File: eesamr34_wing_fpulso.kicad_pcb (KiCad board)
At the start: 2 copper layers, 50 x 24.9 mm, 19 parts, among them J3 Conn_01x02_Male, P1 SolderJumper_3_Bridged12, Q1 BS250, U2 4069

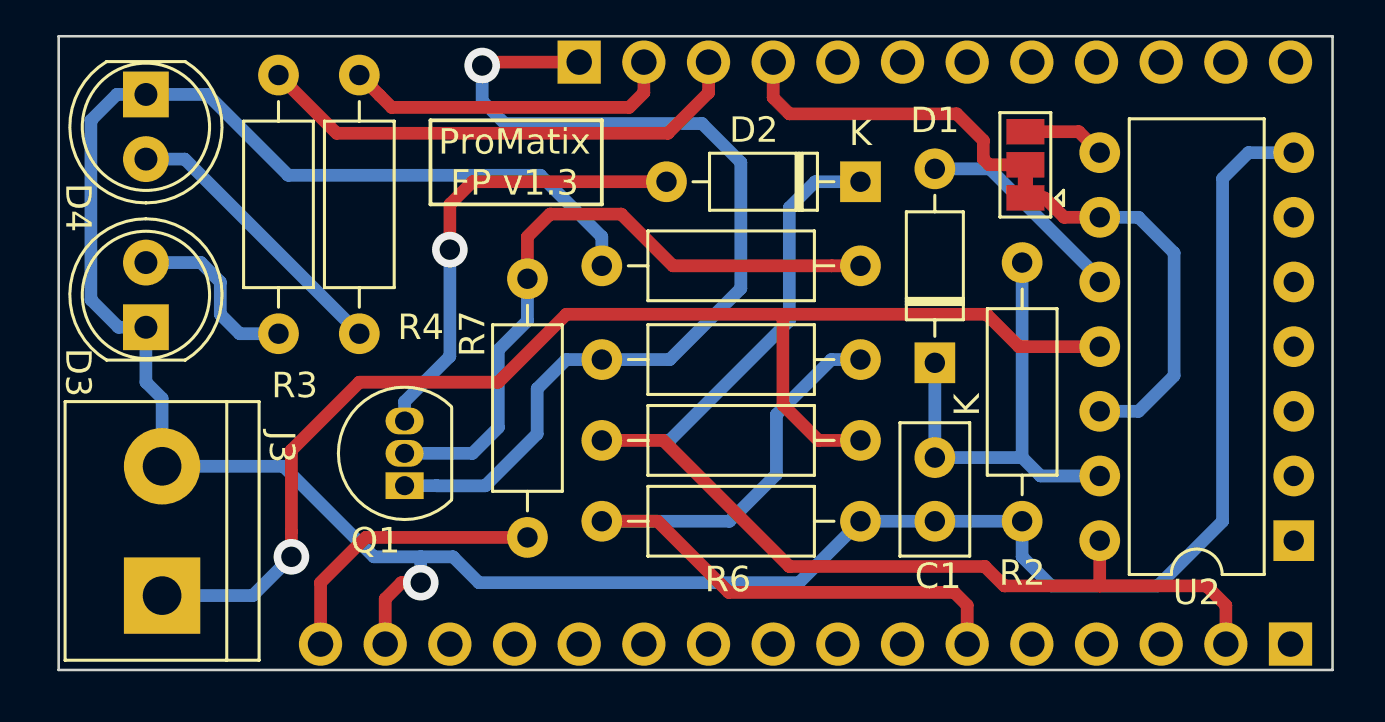
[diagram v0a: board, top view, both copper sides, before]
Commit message: entradas no usadas a 0
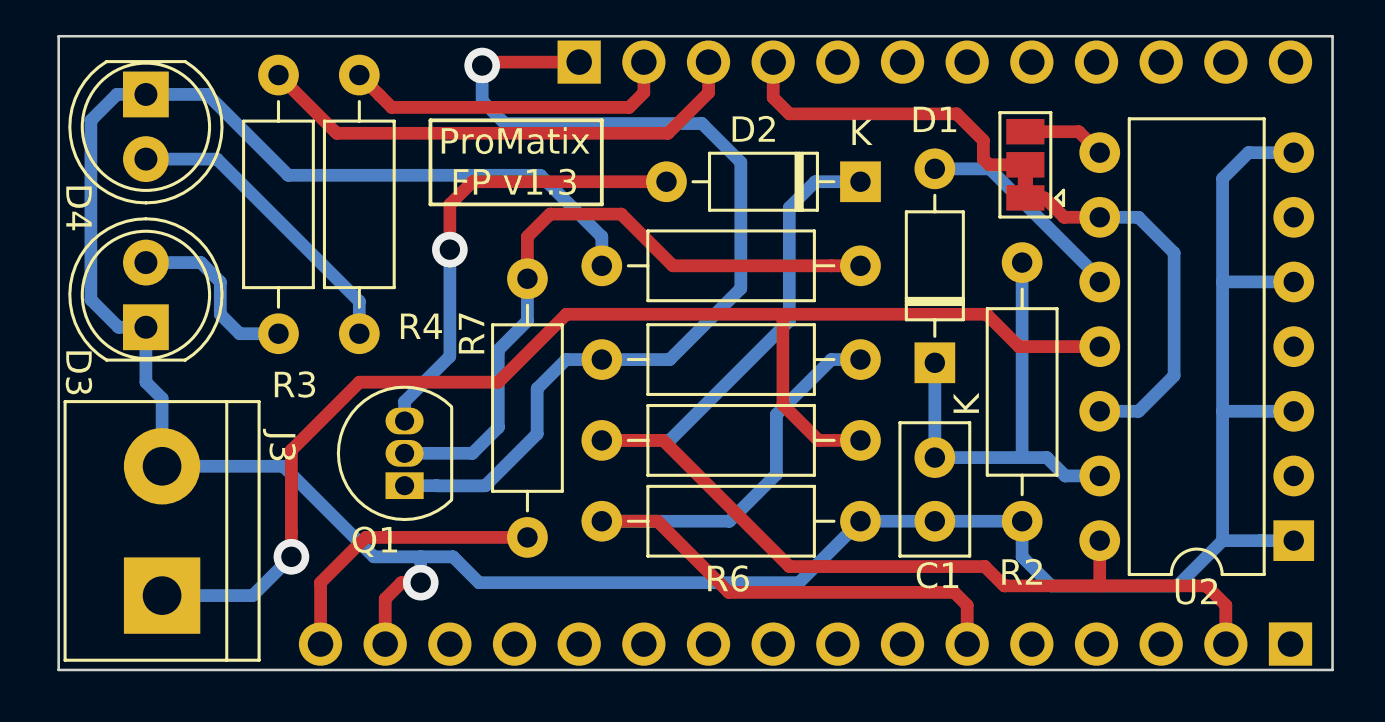
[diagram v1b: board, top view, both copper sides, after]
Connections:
- U2 pad 1: Net-(U2-Pad1) -> GND
- U2 pad 3: Net-(U2-Pad3) -> GND
- U2 pad 5: Net-(U2-Pad5) -> GND
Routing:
- net GND: track 107.9 -> 116.8 mm
- net Net-(D4-Pad2): track 11.2 -> 12.0 mm
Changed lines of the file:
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@@
     (thickness 1.6)
     (drawings 12)
-    (tracks 153)
+    (tracks 161)
     (zones 0)
     (modules 19)
-    (nets 44)
+    (nets 41)
   )
   (page A4 portrait)
@@
     (0 F.Cu signal)
     (31 B.Cu signal)
-    (32 B.Adhes user hide)
-    (33 F.Adhes user hide)
-    (34 B.Paste user hide)
-    (35 F.Paste user hide)
+    (32 B.Adhes user)
+    (33 F.Adhes user)
+    (34 B.Paste user)
+    (35 F.Paste user)
     (36 B.SilkS user)
     (37 F.SilkS user)
     (38 B.Mask user)
-    (39 F.Mask user hide)
+    (39 F.Mask user)
     (40 Dwgs.User user)
     (41 Cmts.User user)
@@
     (43 Eco2.User user)
     (44 Edge.Cuts user)
-    (45 Margin user hide)
+    (45 Margin user)
     (46 B.CrtYd user)
     (47 F.CrtYd user)
-    (48 B.Fab user hide)
-    (49 F.Fab user hide)
+    (48 B.Fab user)
+    (49 F.Fab user)
   )
   (setup
-    (last_trace_width 0.8)
+    (last_trace_width 0.5)
     (user_trace_width 0.5)
     (user_trace_width 0.8)
@@
   (net 36 /ADC7)
   (net 37 "Net-(Q1-Pad2)")
-  (net 38 "Net-(U2-Pad3)")
-  (net 39 "Net-(U2-Pad4)")
-  (net 40 "Net-(U2-Pad1)")
-  (net 41 "Net-(U2-Pad2)")
-  (net 42 "Net-(U2-Pad5)")
-  (net 43 "Net-(U2-Pad6)")
+  (net 38 "Net-(U2-Pad4)")
+  (net 39 "Net-(U2-Pad2)")
+  (net 40 "Net-(U2-Pad6)")
   (net_class Default "This is the default net class."
     (clearance 0.4)
@@
     (add_net "Net-(P1-Pad3)")
     (add_net "Net-(Q1-Pad2)")
-    (add_net "Net-(U2-Pad1)")
     (add_net "Net-(U2-Pad2)")
-    (add_net "Net-(U2-Pad3)")
     (add_net "Net-(U2-Pad4)")
-    (add_net "Net-(U2-Pad5)")
     (add_net "Net-(U2-Pad6)")
   )
@@
     )
     (pad 1 thru_hole rect (at 0 0 180) (size 1.6 1.6) (drill 0.8) (layers *.Cu *.Mask)
-      (net 40 "Net-(U2-Pad1)"))
+      (net 1 GND))
     (pad 8 thru_hole oval (at 7.62 15.24 180) (size 1.6 1.6) (drill 0.8) (layers *.Cu *.Mask)
       (net 7 "Net-(P1-Pad3)"))
     (pad 2 thru_hole oval (at 0 2.54 180) (size 1.6 1.6) (drill 0.8) (layers *.Cu *.Mask)
-      (net 41 "Net-(U2-Pad2)"))
+      (net 39 "Net-(U2-Pad2)"))
     (pad 9 thru_hole oval (at 7.62 12.7 180) (size 1.6 1.6) (drill 0.8) (layers *.Cu *.Mask)
       (net 6 "Net-(P1-Pad1)"))
     (pad 3 thru_hole oval (at 0 5.08 180) (size 1.6 1.6) (drill 0.8) (layers *.Cu *.Mask)
-      (net 38 "Net-(U2-Pad3)"))
+      (net 1 GND))
     (pad 10 thru_hole oval (at 7.62 10.16 180) (size 1.6 1.6) (drill 0.8) (layers *.Cu *.Mask)
       (net 4 "Net-(D1-Pad2)"))
     (pad 4 thru_hole oval (at 0 7.62 180) (size 1.6 1.6) (drill 0.8) (layers *.Cu *.Mask)
-      (net 39 "Net-(U2-Pad4)"))
+      (net 38 "Net-(U2-Pad4)"))
     (pad 11 thru_hole oval (at 7.62 7.62 180) (size 1.6 1.6) (drill 0.8) (layers *.Cu *.Mask)
       (net 35 /Pulse))
     (pad 5 thru_hole oval (at 0 10.16 180) (size 1.6 1.6) (drill 0.8) (layers *.Cu *.Mask)
-      (net 42 "Net-(U2-Pad5)"))
+      (net 1 GND))
     (pad 12 thru_hole oval (at 7.62 5.08 180) (size 1.6 1.6) (drill 0.8) (layers *.Cu *.Mask)
       (net 6 "Net-(P1-Pad1)"))
     (pad 6 thru_hole oval (at 0 12.7 180) (size 1.6 1.6) (drill 0.8) (layers *.Cu *.Mask)
-      (net 43 "Net-(U2-Pad6)"))
+      (net 40 "Net-(U2-Pad6)"))
     (pad 13 thru_hole oval (at 7.62 2.54 180) (size 1.6 1.6) (drill 0.8) (layers *.Cu *.Mask)
       (net 3 "Net-(C1-Pad1)"))
@@
   (segment (start 105.537 140.716) (end 108.458 140.716) (width 0.5) (layer B.Cu) (net 1))
   (segment (start 108.458 140.716) (end 111.887 140.716) (width 0.5) (layer B.Cu) (net 1))
-  (segment (start 111.887 142.113) (end 111.887 140.716) (width 0.5) (layer B.Cu) (net 1))
-  (segment (start 113.03 143.256) (end 111.887 142.113) (width 0.5) (layer B.Cu) (net 1))
-  (segment (start 122.555 126.238) (end 120.777 126.238) (width 0.5) (layer B.Cu) (net 1))
-  (segment (start 119.761 127.254) (end 119.761 140.716) (width 0.5) (layer B.Cu) (net 1))
-  (segment (start 120.777 126.238) (end 119.761 127.254) (width 0.5) (layer B.Cu) (net 1))
-  (segment (start 119.761 140.716) (end 117.221 143.256) (width 0.5) (layer B.Cu) (net 1))
-  (segment (start 117.221 143.256) (end 113.03 143.256) (width 0.5) (layer B.Cu) (net 1))
-  (segment (start 79.883 123.952) (end 77.47 123.952) (width 0.5) (layer B.Cu) (net 1))
-  (segment (start 83.058 127.127) (end 79.883 123.952) (width 0.5) (layer B.Cu) (net 1))
-  (segment (start 92.964 127.127) (end 83.058 127.127) (width 0.5) (layer B.Cu) (net 1))
-  (segment (start 95.377 130.683) (end 95.377 129.54) (width 0.5) (layer B.Cu) (net 1))
-  (segment (start 95.377 129.54) (end 92.964 127.127) (width 0.5) (layer B.Cu) (net 1))
   (segment (start 86.868 143.764) (end 87.503 143.129) (width 0.5) (layer F.Cu) (net 1))
   (segment (start 86.868 145.542) (end 86.868 143.764) (width 0.5) (layer F.Cu) (net 1))
@@
   (segment (start 82.8675 138.557) (end 78.105 138.557) (width 0.5) (layer B.Cu) (net 1))
   (segment (start 86.4235 142.113) (end 82.8675 138.557) (width 0.5) (layer B.Cu) (net 1))
-  (segment (start 78.105 135.89) (end 77.47 135.255) (width 0.5) (layer B.Cu) (net 1) (status 1000000))
-  (segment (start 77.47 135.255) (end 77.47 133.096) (width 0.5) (layer B.Cu) (net 1) (status 1000000))
-  (segment (start 78.105 138.557) (end 78.105 135.89) (width 0.5) (layer B.Cu) (net 1) (status 1000000))
-  (segment (start 76.3905 133.096) (end 77.47 133.096) (width 0.5) (layer B.Cu) (net 1) (status 1000000))
-  (segment (start 76.327 123.952) (end 75.311 124.968) (width 0.5) (layer B.Cu) (net 1) (status 1000000))
-  (segment (start 77.47 123.952) (end 76.327 123.952) (width 0.5) (layer B.Cu) (net 1) (status 1000000))
-  (segment (start 75.311 124.968) (end 75.311 132.0165) (width 0.5) (layer B.Cu) (net 1) (status 1000000))
-  (segment (start 75.311 132.0165) (end 76.3905 133.096) (width 0.5) (layer B.Cu) (net 1) (status 1000000))
-  (segment (start 111.887 138.216) (end 108.458 138.216) (width 0.5) (layer B.Cu) (net 3))
-  (segment (start 112.609 138.938) (end 114.935 138.938) (width 0.5) (layer B.Cu) (net 3))
-  (segment (start 111.887 138.216) (end 112.609 138.938) (width 0.5) (layer B.Cu) (net 3))
+  (segment (start 78.105 135.89) (end 77.47 135.255) (width 0.5) (layer B.Cu) (net 1))
+  (segment (start 77.47 135.255) (end 77.47 133.096) (width 0.5) (layer B.Cu) (net 1))
+  (segment (start 78.105 138.557) (end 78.105 135.89) (width 0.5) (layer B.Cu) (net 1))
+  (segment (start 76.3905 133.096) (end 77.47 133.096) (width 0.5) (layer B.Cu) (net 1))
+  (segment (start 76.327 123.952) (end 75.311 124.968) (width 0.5) (layer B.Cu) (net 1))
+  (segment (start 77.47 123.952) (end 76.327 123.952) (width 0.5) (layer B.Cu) (net 1))
+  (segment (start 75.311 124.968) (end 75.311 132.0165) (width 0.5) (layer B.Cu) (net 1))
+  (segment (start 75.311 132.0165) (end 76.3905 133.096) (width 0.5) (layer B.Cu) (net 1))
+  (segment (start 92.964 127.127) (end 83.058 127.127) (width 0.5) (layer B.Cu) (net 1))
+  (segment (start 95.377 129.54) (end 92.964 127.127) (width 0.5) (layer B.Cu) (net 1))
+  (segment (start 95.377 130.683) (end 95.377 129.54) (width 0.5) (layer B.Cu) (net 1))
+  (segment (start 83.058 127.127) (end 79.883 123.952) (width 0.5) (layer B.Cu) (net 1))
+  (segment (start 79.883 123.952) (end 77.47 123.952) (width 0.5) (layer B.Cu) (net 1))
+  (segment (start 120.777 126.238) (end 119.761 127.254) (width 0.5) (layer B.Cu) (net 1))
+  (segment (start 113.03 143.256) (end 111.887 142.113) (width 0.5) (layer B.Cu) (net 1))
+  (segment (start 122.555 126.238) (end 120.777 126.238) (width 0.5) (layer B.Cu) (net 1))
+  (segment (start 117.983 143.256) (end 113.03 143.256) (width 0.5) (layer B.Cu) (net 1))
+  (segment (start 111.887 142.113) (end 111.887 140.716) (width 0.5) (layer B.Cu) (net 1))
+  (segment (start 119.761 141.478) (end 117.983 143.256) (width 0.5) (layer B.Cu) (net 1))
+  (segment (start 121.255 141.478) (end 119.761 141.478) (width 0.5) (layer B.Cu) (net 1))
+  (segment (start 122.555 141.478) (end 121.255 141.478) (width 0.5) (layer B.Cu) (net 1))
+  (segment (start 121.42363 136.398) (end 119.761 136.398) (width 0.5) (layer B.Cu) (net 1))
+  (segment (start 122.555 136.398) (end 121.42363 136.398) (width 0.5) (layer B.Cu) (net 1))
+  (segment (start 119.761 136.398) (end 119.761 141.478) (width 0.5) (layer B.Cu) (net 1))
+  (segment (start 119.761 127.254) (end 119.761 131.318) (width 0.5) (layer B.Cu) (net 1))
+  (segment (start 122.555 131.318) (end 119.761 131.318) (width 0.5) (layer B.Cu) (net 1))
+  (segment (start 119.761 131.318) (end 119.761 136.398) (width 0.5) (layer B.Cu) (net 1))
   (segment (start 111.887 130.556) (end 111.887 138.176) (width 0.5) (layer B.Cu) (net 3))
   (segment (start 108.458 138.216) (end 108.458 134.493) (width 0.5) (layer B.Cu) (net 3))
+  (segment (start 113.5815 138.938) (end 114.935 138.938) (width 0.5) (layer B.Cu) (net 3))
+  (segment (start 108.458 138.216) (end 112.8595 138.216) (width 0.5) (layer B.Cu) (net 3))
+  (segment (start 112.8595 138.216) (end 113.5815 138.938) (width 0.5) (layer B.Cu) (net 3))
   (segment (start 114.935 131.191) (end 114.935 131.318) (width 0.5) (layer B.Cu) (net 4))
   (segment (start 108.458 126.873) (end 110.617 126.873) (width 0.5) (layer B.Cu) (net 4))
@@
   (segment (start 80.391 131.318) (end 80.391 132.588) (width 0.5) (layer B.Cu) (net 33))
   (segment (start 79.629 130.556) (end 80.391 131.318) (width 0.5) (layer B.Cu) (net 33))
-  (segment (start 78.994 126.492) (end 85.852 133.35) (width 0.5) (layer B.Cu) (net 34))
-  (segment (start 77.47 126.492) (end 78.994 126.492) (width 0.5) (layer B.Cu) (net 34))
+  (segment (start 85.852 132.08) (end 85.852 133.35) (width 0.5) (layer B.Cu) (net 34))
+  (segment (start 77.47 126.492) (end 80.264 126.492) (width 0.5) (layer B.Cu) (net 34))
+  (segment (start 80.264 126.492) (end 85.852 132.08) (width 0.5) (layer B.Cu) (net 34))
   (segment (start 81.661 143.637) (end 83.185 142.113) (width 0.5) (layer B.Cu) (net 35))
   (segment (start 78.105 143.637) (end 81.661 143.637) (width 0.5) (layer B.Cu) (net 35))

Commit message: cambios menores
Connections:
- P1 pad 2: /I2C_SDa -> /SPI_MOSI
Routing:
- net /I2C_SDa: track 12.8 -> 0.00 mm
- net /SPI_MOSI: track 0.00 -> 5.52 mm
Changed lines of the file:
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@@
     (thickness 1.6)
     (drawings 12)
-    (tracks 161)
+    (tracks 158)
     (zones 0)
     (modules 19)
@@
       (net 7 "Net-(P1-Pad3)"))
     (pad 2 smd rect (at 0 0 90) (size 1 1.5) (layers F.Cu F.Mask)
-      (net 26 /I2C_SDa))
+      (net 29 /SPI_MOSI))
   )
   (module Resistor_THT:R_Axial_DIN0207_L6.3mm_D2.5mm_P10.16mm_Horizontal (layer F.Cu)
@@
   (segment (start 82.677 123.19) (end 84.963 125.476) (width 0.5) (layer F.Cu) (net 25))
   (segment (start 84.963 125.476) (end 97.976081 125.476) (width 0.5) (layer F.Cu) (net 25))
-  (segment (start 110.587 126.716) (end 112.014 126.716) (width 0.5) (layer F.Cu) (net 26))
-  (segment (start 110.363 126.492) (end 110.587 126.716) (width 0.5) (layer F.Cu) (net 26))
-  (segment (start 102.108 124.079) (end 102.743 124.714) (width 0.5) (layer F.Cu) (net 26))
-  (segment (start 109.317 124.714) (end 110.363 125.76) (width 0.5) (layer F.Cu) (net 26))
-  (segment (start 102.108 122.682) (end 102.108 124.079) (width 0.5) (layer F.Cu) (net 26))
-  (segment (start 102.743 124.714) (end 109.317 124.714) (width 0.5) (layer F.Cu) (net 26))
-  (segment (start 110.363 125.76) (end 110.363 126.492) (width 0.5) (layer F.Cu) (net 26))
+  (segment (start 109.728 123.884081) (end 109.728 122.682) (width 0.5) (layer F.Cu) (net 29))
+  (segment (start 109.728 125.349) (end 109.728 123.884081) (width 0.5) (layer F.Cu) (net 29))
+  (segment (start 112.014 126.716) (end 111.095 126.716) (width 0.5) (layer F.Cu) (net 29))
+  (segment (start 111.095 126.716) (end 109.728 125.349) (width 0.5) (layer F.Cu) (net 29))
   (segment (start 81.153 133.35) (end 82.677 133.35) (width 0.5) (layer B.Cu) (net 33))
   (segment (start 80.391 132.588) (end 81.153 133.35) (width 0.5) (layer B.Cu) (net 33))
